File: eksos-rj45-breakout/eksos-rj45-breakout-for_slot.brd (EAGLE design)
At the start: 264.5 x 70 mm, 7 parts, among them X1 RJ45-8X-DS1130, X2 RJ45-8X-DS1130

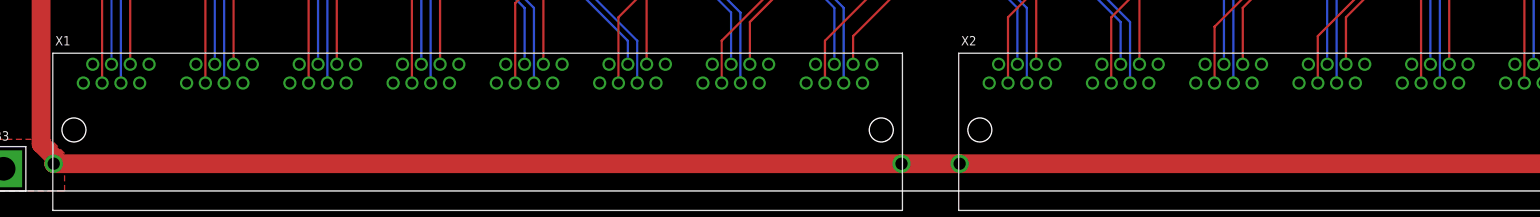
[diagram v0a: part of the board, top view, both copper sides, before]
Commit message: eksos-rj45-breakout: Update DS1130 library (3 more SHLD, 1 more drill)
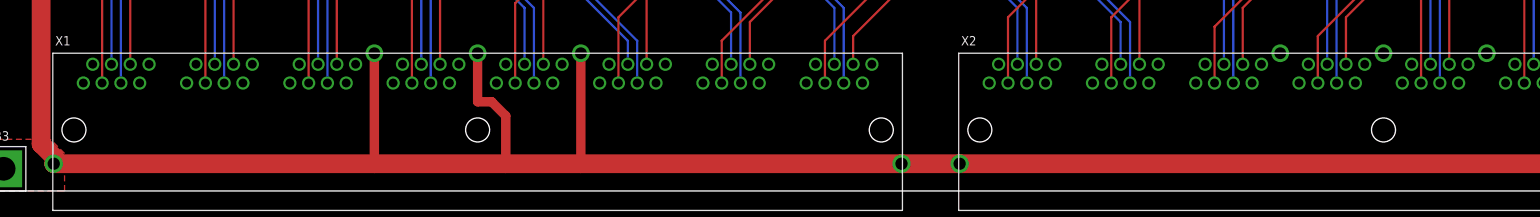
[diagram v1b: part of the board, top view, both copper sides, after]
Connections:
- net SHLD: now also X1.SHLD3, X1.SHLD4, X1.SHLD5, X2.SHLD3, X2.SHLD4, X2.SHLD5
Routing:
- net SHLD: track 541.6 -> 589.1 mm
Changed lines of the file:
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@@
 <wire x1="13.775" y1="3.685" x2="13.97" y2="3.88" width="2.54" layer="1"/>
 <wire x1="15.875" y1="60.96" x2="109.22" y2="60.96" width="2.54" layer="1"/>
-<wire x1="128.465" y1="3.685" x2="13.775" y2="3.685" width="2.54" layer="1"/>
+<wire x1="128.465" y1="3.685" x2="85.09" y2="3.685" width="2.54" layer="1"/>
+<wire x1="85.09" y1="3.685" x2="74.93" y2="3.685" width="2.54" layer="1"/>
+<wire x1="74.93" y1="3.685" x2="57.15" y2="3.685" width="2.54" layer="1"/>
+<wire x1="57.15" y1="3.685" x2="13.775" y2="3.685" width="2.54" layer="1"/>
 <wire x1="128.465" y1="3.685" x2="136.33" y2="3.685" width="2.54" layer="1"/>
 <wire x1="136.33" y1="3.685" x2="251.02" y2="3.685" width="2.54" layer="1"/>
@@
 <vertex x="250.19" y="0"/>
 </polygon>
+<contactref element="X1" pad="SHLD3"/>
+<contactref element="X1" pad="SHLD4"/>
+<contactref element="X1" pad="SHLD5"/>
+<contactref element="X2" pad="SHLD3"/>
+<contactref element="X2" pad="SHLD4"/>
+<contactref element="X2" pad="SHLD5"/>
+<wire x1="57.15" y1="18.635" x2="57.15" y2="3.685" width="1.27" layer="1"/>
+<wire x1="85.09" y1="18.635" x2="85.09" y2="3.685" width="1.27" layer="1"/>
+<wire x1="71.12" y1="18.635" x2="71.12" y2="12.065" width="1.27" layer="1"/>
+<wire x1="71.12" y1="12.065" x2="73.025" y2="12.065" width="1.27" layer="1"/>
+<wire x1="73.025" y1="12.065" x2="74.93" y2="10.16" width="1.27" layer="1"/>
+<wire x1="74.93" y1="10.16" x2="74.93" y2="3.685" width="1.27" layer="1"/>
+<wire x1="193.675" y1="18.635" x2="207.645" y2="18.635" width="0" layer="19" extent="1-1"/>
+<wire x1="179.705" y1="18.635" x2="193.675" y2="18.635" width="0" layer="19" extent="1-1"/>
+<wire x1="179.705" y1="54.61" x2="179.705" y2="18.635" width="0" layer="19" extent="1-1"/>
 </signal>
 <signal name="B1C">

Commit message: eksos-rj45-breakout-for_slot: Move IDC connectors 11mm towards edge
It turns out that it's not very easy to bend the 64pos ribbon cable,
so let's make sure the IDC connectors align with  the plane of the
ribbon cable from the PSTN/ISDN line cards.
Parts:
- moved SV1 10.8 mm to (60.3, 54.6)
- moved SV2 10.2 mm to (203.8, 53.3)
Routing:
- net SHLD: track 589.1 -> 626.0 mm
- net 5C: track 144.3 -> 155.5 mm
- net 3A: track 145.4 -> 156.5 mm
- net 15A: track 89.4 -> 100.6 mm
- net 15C: track 95.0 -> 106.2 mm
- net 21C: track 55.7 -> 66.9 mm
- net 5A: track 138.7 -> 149.9 mm
- net 7C: track 136.2 -> 147.0 mm
- net 7A: track 130.6 -> 141.3 mm
- net 3C: track 151.0 -> 161.8 mm
- net 21A: track 50.1 -> 60.9 mm
- net 1C: track 153.2 -> 164.0 mm
- net 1A: track 148.3 -> 159.1 mm
- net B31C: track 165.3 -> 175.8 mm
- net B31A: track 168.0 -> 178.2 mm
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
